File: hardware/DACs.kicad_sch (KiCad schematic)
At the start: 70 parts, among them U10 LT1678CS8#PBF, U11 LT1678CS8#PBF, U12 LT1678CS8#PBF, U13 LT1678CS8#PBF, U14 LT1461CIS8-2.5#PBF, U6 LTC2642ACDD-16#PBF, U7 LTC2642ACDD-16#PBF, U8 LTC2642ACDD-16#PBF, U9 LTC2642ACDD-16#PBF

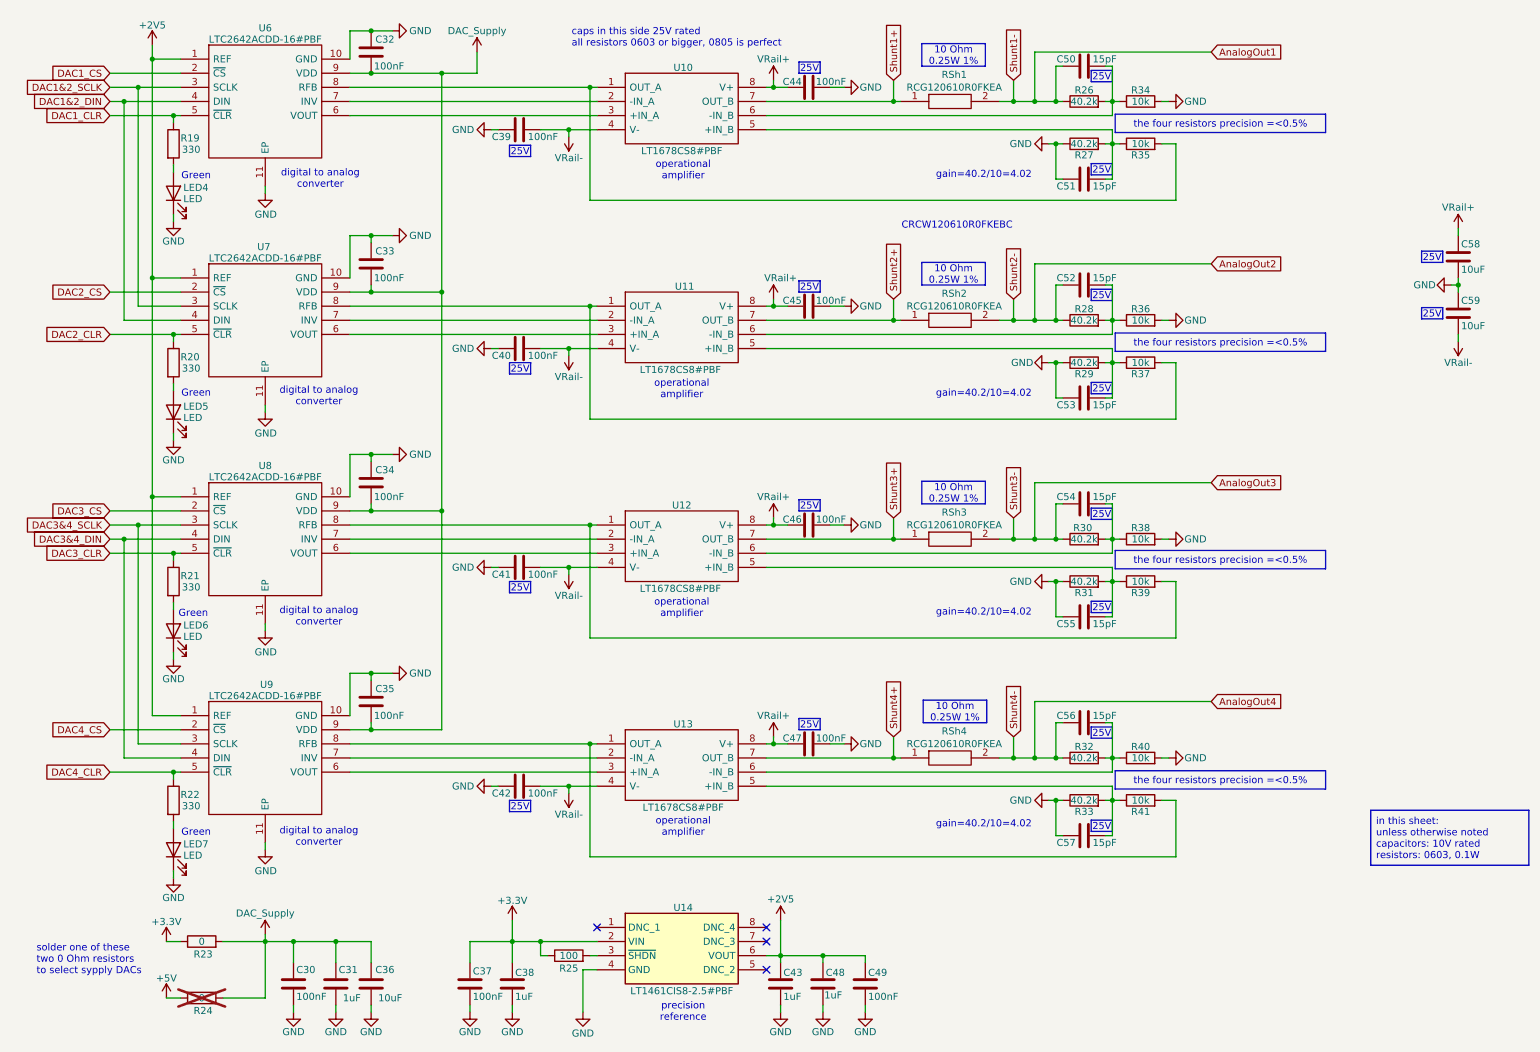
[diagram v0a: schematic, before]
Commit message: draft new analog signal chain & short-circuit detection
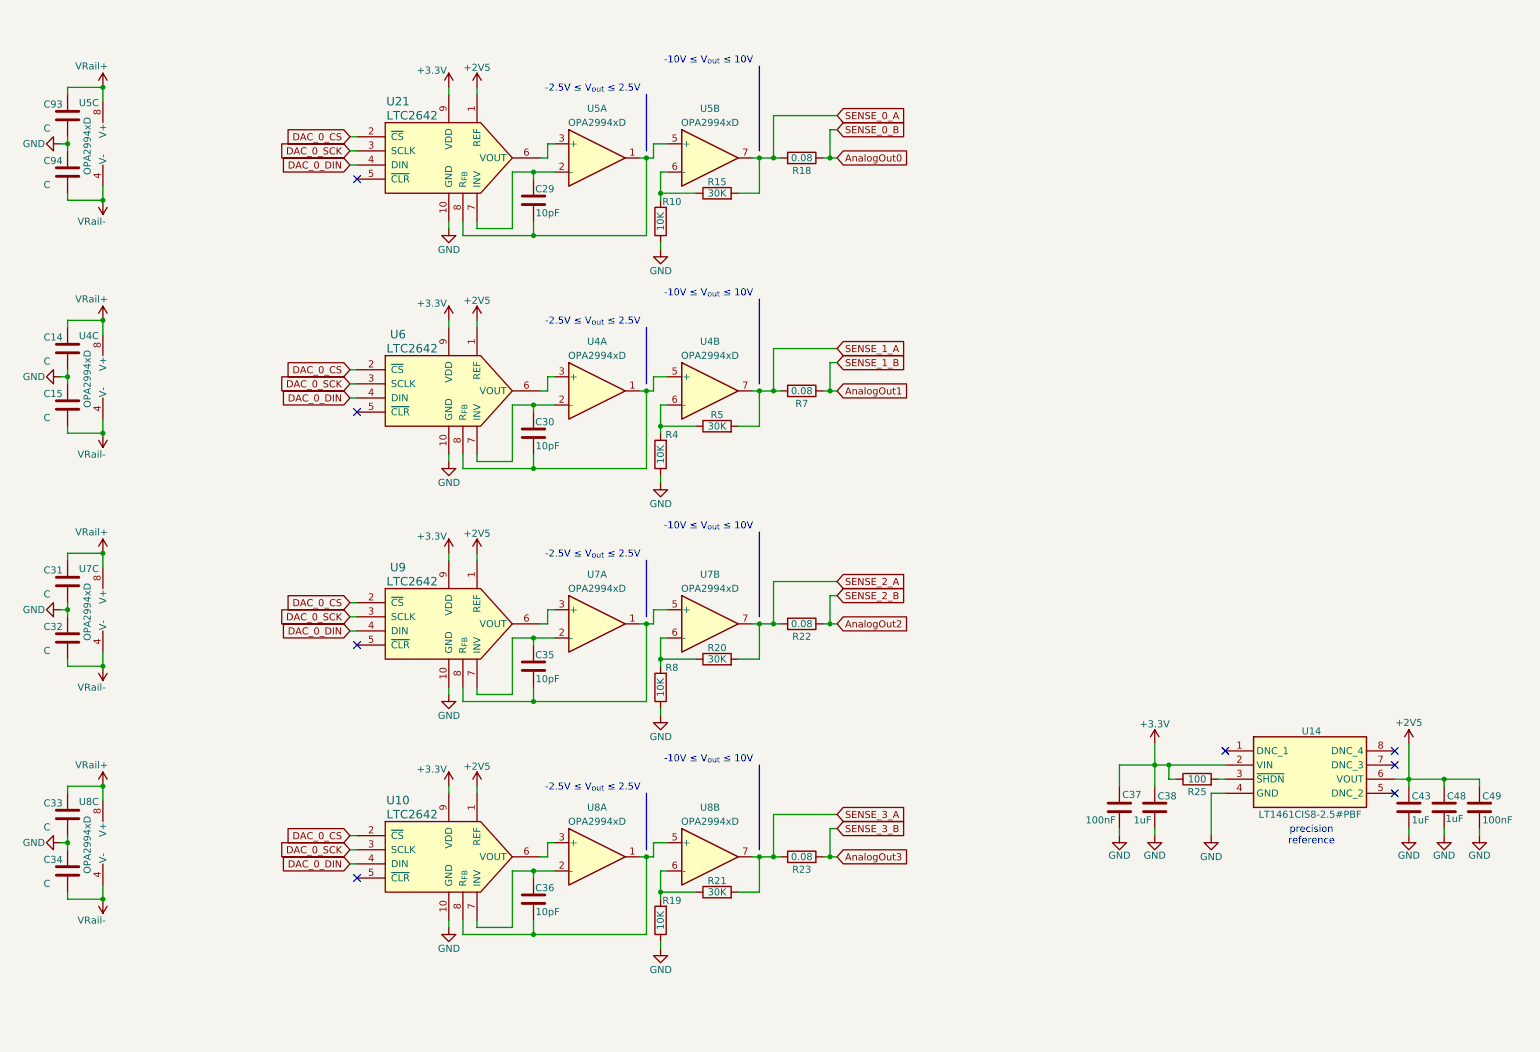
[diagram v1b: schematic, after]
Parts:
- removed C30, C32, C33, C34, C35, C39, C40, C41, C42, C44, C45, C46, C47: 100nF, Capacitor_SMD:C_0603_1608Metric, symbol harp.device.quad.dac:C_0603
- removed C31: 1uF, Capacitor_SMD:C_0603_1608Metric, symbol harp.device.quad.dac:C_0603
- removed C36, C58, C59: 10uF, Capacitor_SMD:C_0603_1608Metric, symbol harp.device.quad.dac:C_0603
- removed C50, C51, C52, C53, C54, C55, C56, C57: 15pF, Capacitor_SMD:C_0603_1608Metric, symbol harp.device.quad.dac:C_0603
- removed LED4, LED5, LED6, LED7: LED, harp.device.quad.dac.kicad:LED_0603_1608Metric_Pad1.05x0.95mm_HandSolder, symbol harp.device.quad.dac:LED
- removed R19, R20, R21, R22: 330, Resistor_SMD:R_0603_1608Metric, symbol harp.device.quad.dac:R_0603
- removed R23, R24: 0, Resistor_SMD:R_0603_1608Metric, symbol harp.device.quad.dac:R_0603
- removed R26, R27, R28, R29, R30, R31, R32, R33: 40.2k, Resistor_SMD:R_0603_1608Metric, symbol harp.device.quad.dac:R_0603
- removed R34, R35, R36, R37, R38, R39, R40, R41: 10k, Resistor_SMD:R_0603_1608Metric, symbol harp.device.quad.dac:R_0603
- removed RSh1, RSh2, RSh3, RSh4: RCG120610R0FKEA, Resistor_SMD:R_1206_3216Metric, symbol harp.device.quad.dac:CRCW120610R0FKEBC
- removed U10, U11, U12, U13: LT1678CS8#PBF, harp.device.quad.dac.kicad:SOIC127P599X175-8N, symbol harp.device.quad.dac:LT1678CS8#PBF
- removed U6, U7, U8, U9: LTC2642ACDD-16#PBF, harp.device.quad.dac.kicad:SON50P300X300X80-11N-D, symbol harp.device.quad.dac:LTC2642ACDD-16#PBF
- added C14, C15, C31, C32, C33, C34, C93, C94: C, symbol Device:C
- added C29, C30, C35, C36: 10pF, symbol Device:C
- added R10, R19, R4, R8: 10K, symbol Device:R
- added R15, R20, R21, R5: 30K, symbol Device:R
- added R18, R22, R23, R7: 0.08, symbol Device:R
- added U10, U21, U6, U9: LTC2642, symbol kicad_component_library:LTC2642
- added U4, U5, U7, U8: OPA2994xD, Package_SO:SOIC-8_3.9x4.9mm_P1.27mm, symbol Amplifier_Operational:OPA2994xD
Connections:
- net +2V5: now also U10.1 (REF), U21.1 (REF), U6.1 (REF), U9.1 (REF)
- net +3.3V: now also U10.9 (VDD), U21.9 (VDD), U6.9 (VDD), U9.9 (VDD)
- net AnalogOut1: now also R7.1
- net AnalogOut2: now also R22.1
- net AnalogOut3: now also R23.1
- net GND: now also C14.2, C15.1, C31.2, C32.1, C33.2, C34.1, C93.2, C94.1, R10.1, R19.1, R4.1, R8.1, U10.10 (GND), U21.10 (GND), U6.10 (GND), U9.10 (GND)
- net VRail+: now also C14.1, C31.1, C33.1, C93.1, U4.8 (V+), U5.8 (V+), U7.8 (V+), U8.8 (V+)
- net VRail-: now also C15.2, C32.2, C34.2, C94.2, U4.4 (V-), U5.4 (V-), U7.4 (V-), U8.4 (V-)
- new net: R20.1, R8.2, U7.6 (-)
- new net: R10.2, R15.1, U5.6 (-)
- new net: R4.2, R5.1, U4.6 (-)
- new net: R19.2, R21.1, U8.6 (-)
- new net: C35.1, U7.1, U7.5 (+), U9.8 (R_{FB})
- new net: C30.1, U4.1, U4.5 (+), U6.8 (R_{FB})
- new net: C30.2, U4.2 (-), U6.7 (INV)
- new net: U4.3 (+), U6.6 (VOUT)
- new net: C29.1, U21.8 (R_{FB}), U5.1, U5.5 (+)
- new net: C29.2, U21.7 (INV), U5.2 (-)
- new net: C35.2, U7.2 (-), U9.7 (INV)
- new net: U7.3 (+), U9.6 (VOUT)
- new net: U10.6 (VOUT), U8.3 (+)
- new net: C36.2, U10.7 (INV), U8.2 (-)
- new net: C36.1, U10.8 (R_{FB}), U8.1, U8.5 (+)
- new net: U21.6 (VOUT), U5.3 (+)
- new net AnalogOut0: R18.1
- new net DAC_0_CS: U10.2 (~{CS}), U21.2 (~{CS}), U6.2 (~{CS}), U9.2 (~{CS})
- new net DAC_0_DIN: U10.4 (DIN), U21.4 (DIN), U6.4 (DIN), U9.4 (DIN)
- new net DAC_0_SCK: U10.3 (SCLK), U21.3 (SCLK), U6.3 (SCLK), U9.3 (SCLK)
- new net SENSE_0_A: R15.2, R18.2, U5.7
- new net SENSE_1_A: R5.2, R7.2, U4.7
- new net SENSE_2_A: R20.2, R22.2, U7.7
- new net SENSE_3_A: R21.2, R23.2, U8.7
- no-connect marks 4 -> 8
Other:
- note added: "-10V ≤ V_{out} ≤ 10V"
- note added: "-2.5V ≤ V_{out} ≤ 2.5V"
- note removed: "CRCW120610R0FKEBC"
- note removed: "Green"
- note removed: "caps in this side 25V rated all resistors 0603 or bigger, 0805 is perfect"
- note removed: "digital to analog converter"
- note removed: "gain=40.2/10=4.02"
- note removed: "operational amplifier"
- note removed: "solder one of these two 0 Ohm resistors to select sypply DACs"
- moved on the sheet: C37, C38, C43, C48, C49, R25, U14

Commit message: draft split rail power supply design
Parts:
- R18, R22, R23, R7: value 0.08 -> 0.05
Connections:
- net VRail+ renamed +12V
- net VRail- renamed -12V

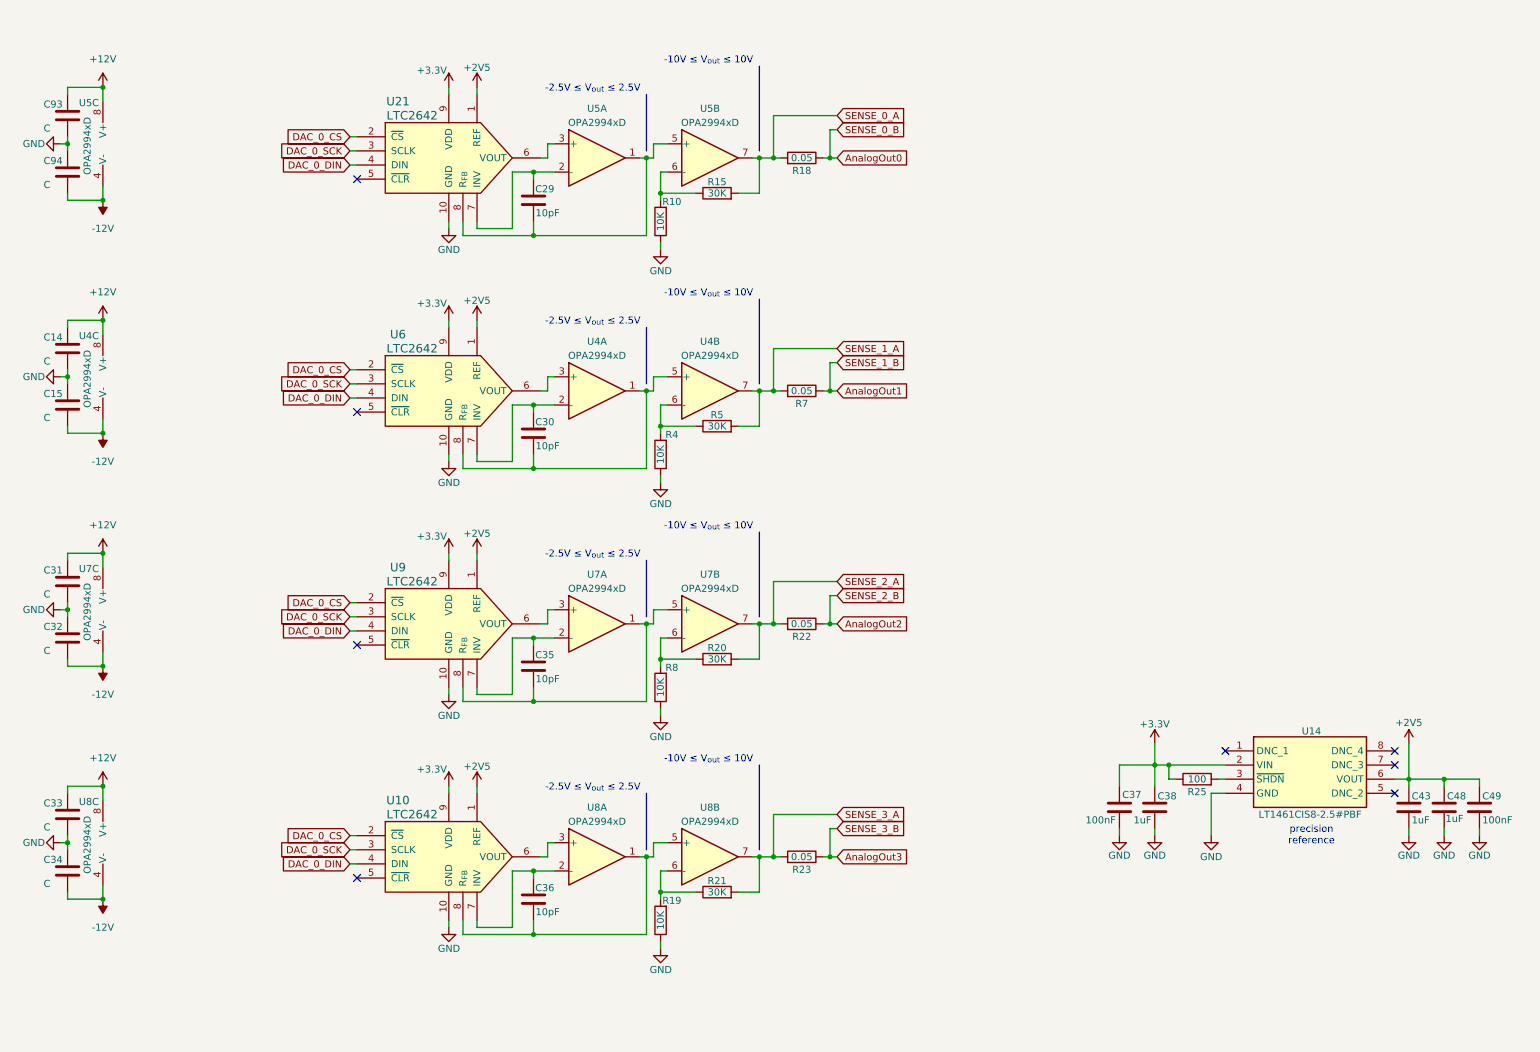
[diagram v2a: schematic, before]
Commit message: update tvs diodes, regulators, and power supply chain
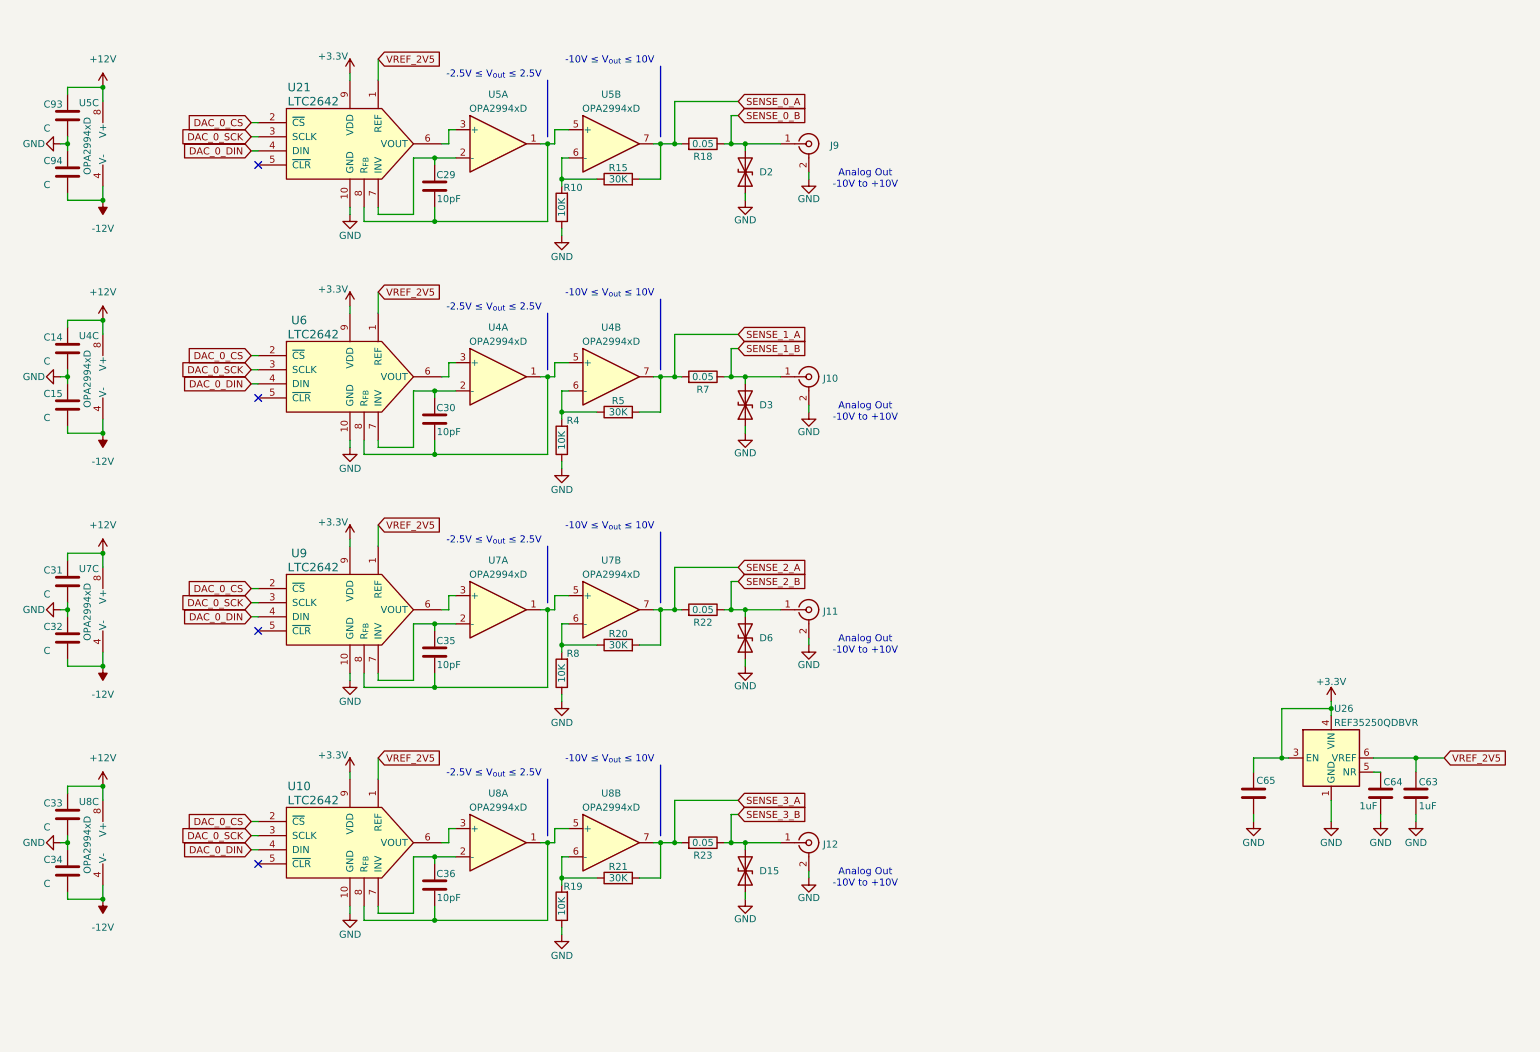
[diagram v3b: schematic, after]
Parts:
- removed C37, C49: 100nF, Capacitor_SMD:C_0603_1608Metric, symbol harp.device.quad.dac:C_0603
- removed C38, C43, C48: 1uF, Capacitor_SMD:C_0603_1608Metric, symbol harp.device.quad.dac:C_0603
- removed R25: 100, Resistor_SMD:R_0603_1608Metric, symbol harp.device.quad.dac:R_0603
- removed U14: LT1461CIS8-2.5#PBF, harp.device.quad.dac.kicad:SOIC127P599X175-8N, symbol harp.device.quad.dac:LT1461CIS8-2.5#PBF
- added C63, C64: 1uF, Capacitor_SMD:C_0603_1608Metric, symbol harp.device.quad.dac:C_0603
- added C65: 100nF, Capacitor_SMD:C_0603_1608Metric, symbol harp.device.quad.dac:C_0603
- added D15, D2, D3, D6: PESD12VL1BSLAZ, Diode_SMD:D_SOD-882, symbol Device:D_TVS
- added J10, J11, J12, J9: Conn_Coaxial, harp.device.quad.dac.kicad:SMA_TE_Connectivity_CONSMA002-SMD-G-T_Horizontal, symbol harp.device.quad.dac:Conn_Coaxial
- added U26: REF35250QDBVR, Package_TO_SOT_SMD:SOT-23-6, symbol Reference_Voltage:REF35250QDBVR
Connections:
- net +3.3V: now also C65.2, U26.3 (EN), U26.4 (VIN)
- net GND: now also C63.2, C64.2, C65.1, D15.1 (A1), D2.1 (A1), D3.1 (A1), D6.1 (A1), J10.2 (Ext), J11.2 (Ext), J12.2 (Ext), J9.2 (Ext), U26.1 (GND), U26.2 (GND)
- net +2V5 renamed VREF_2V5
- net VREF_2V5: now also C63.1, U26.6 (VREF)
- net AnalogOut0 renamed SENSE_0_B
- net SENSE_0_B: now also D2.2 (A2), J9.1 (In)
- net AnalogOut1 renamed SENSE_1_B
- net SENSE_1_B: now also D3.2 (A2), J10.1 (In)
- net AnalogOut2 renamed SENSE_2_B
- net SENSE_2_B: now also D6.2 (A2), J11.1 (In)
- net AnalogOut3 renamed SENSE_3_B
- net SENSE_3_B: now also D15.2 (A2), J12.1 (In)
- new net: C64.1, U26.5 (NR)
- no-connect marks 8 -> 4
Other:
- note added: "Analog Out -10V to +10V"
- note removed: "precision reference"
- moved on the sheet: C29, C30, C35, C36, R10, R15, R18, R19, R20, R21, R22, R23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
